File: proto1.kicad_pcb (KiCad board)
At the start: 2 copper layers, 75 x 51 mm, 67 parts, among them J1 12402012E212A, J11 TC2030, J12 PA_L, J13 Conn_01x02, J14 PA_L, J15 PA_L, J16 PA_L, J17 PA_L, J18 PA_L, J3 LCD, SW1 RESET, SW2 SW_SPDT, SW3 BOOT, SW4 USR1, SW5 USR2, U1 STM32G0B1CBTx, U3 AP2112K-3.3, U4 MCP6002-xMS, Y2 Crystal

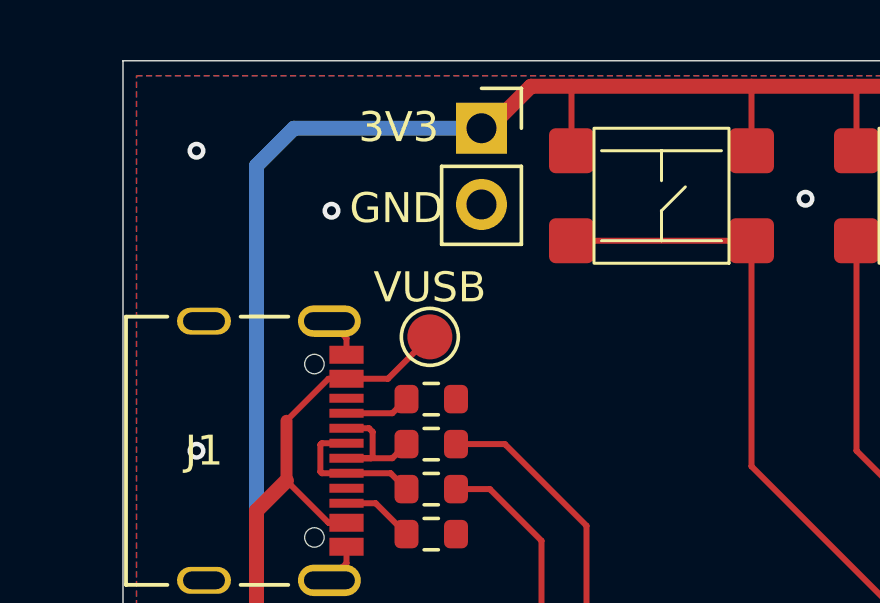
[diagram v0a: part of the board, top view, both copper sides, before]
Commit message: refactor hierarchical sheets to use sheet pins
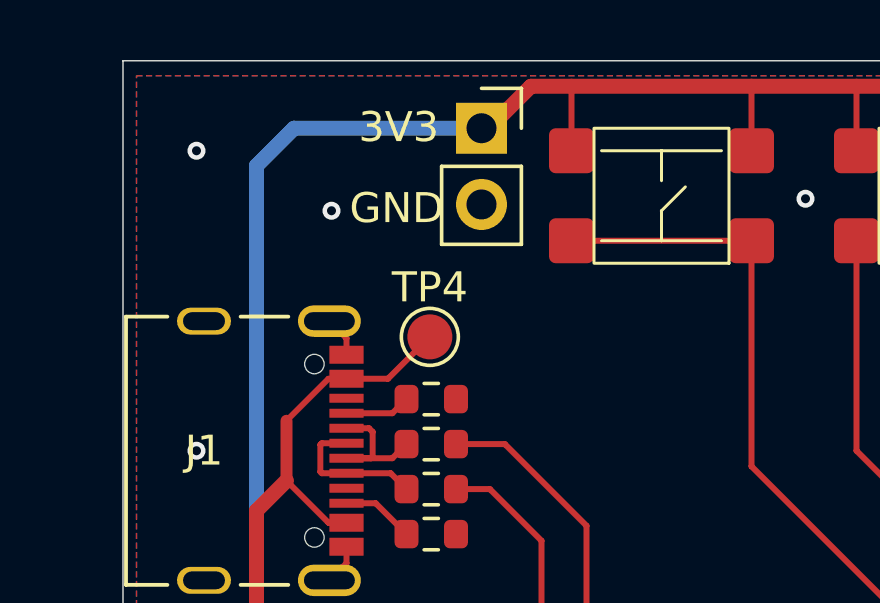
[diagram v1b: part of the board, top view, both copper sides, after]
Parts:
- renumbered VUSB to TP4

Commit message: WIP relayout of board
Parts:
- added AE1: ~, antenna:capacitive_coupled_50mmx8mm, F.Cu at (115.5, 75.5)
- added C17: ~, humidity_sensors:single_layer_comb_34T, B.Cu at (96.5, 57.4)
- C1, C10, C11, C12, C2, C4, C5, C6, C7, C8, C9: footprint Capacitor_SMD:C_0603_1608Metric -> Capacitor_SMD:C_0402_1005Metric
- C3: footprint Capacitor_SMD:C_0402_1005Metric_Pad0.74x0.62mm_HandSolder -> Capacitor_SMD:C_0402_1005Metric
- R1, R10, R11, R12, R13, R14, R15, R16, R18, R19, R2, R20, R21, R22, R23, R24, R3, R4, R5, R6, R8, R9: footprint Resistor_SMD:R_0603_1608Metric -> Resistor_SMD:R_0402_1005Metric
- moved J18 12.4 mm to (72.4, 96.6), turned to 90 degrees
- moved R16 10.0 mm to (93.3, 99.0), turned to 0 degrees
- moved C12 10.0 mm to (93.3, 90.0), turned to 0 degrees
- moved C11 8.05 mm to (98.4, 79.8), turned to 0 degrees
- moved C13 7.68 mm to (88.6, 92.4), turned to 180 degrees
- moved J17 7.65 mm to (69.4, 81.1)
- moved XTAL1 7.44 mm to (87.8, 90.3), turned to 0 degrees
- moved C16 7.23 mm to (83.8, 91.1), turned to 90 degrees
- moved C14 7.17 mm to (87.1, 88.2), turned to 0 degrees
- moved J12 6.99 mm to (84.0, 96.6)
- moved R12 6.90 mm to (102.5, 66.0), turned to 180 degrees
- moved C4 6.66 mm to (87.5, 65.8), turned to -90 degrees
- moved MK1 6.53 mm to (91.1, 65.8), turned to 180 degrees
- moved SW2 6.40 mm to (47.8, 85.6)
- moved J16 6.01 mm to (72.3, 72.5)
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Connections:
- net HUMIDITY_SENSE_COMB renamed /PA1
- net H_COMB_DRIVE renamed Net-(C17-in)
- net MIC_OUT_PDM renamed /PA6
- net NTC_VDIV renamed /PA2
- net SPI1_CLK renamed /PA5
- net cc_antenna_out renamed /PA0
- C7 pad 1: H_COMB_SENSE -> Net-(C17-out)
- J16 pad 6: HUMIDITY_DRIVE_COMB -> /PC6
- R14 pad 2: HUMIDITY_DRIVE_COMB -> /PB15
- U1 pad 30: HUMIDITY_DRIVE_COMB -> /PC6
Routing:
- net H_COMB_SENSE: track 441.7 -> 0.00 mm, vias 1 -> 0
- net Net-(C17-in): track 448.4 -> 24.1 mm
- net +3V3: track 313.7 -> 338.7 mm, vias 5 -> 13
- net Net-(C17-out): track 0.00 -> 12.5 mm, vias 0 -> 1
- net /NRST: track 54.3 -> 41.8 mm, vias 2 -> 0
- net /PA0: track 32.1 -> 20.4 mm
- net /PA2: track 51.0 -> 40.1 mm, vias 2 -> 0
- net HUMIDITY_DRIVE_COMB: track 10.4 -> 0.00 mm
- net /PA1: track 40.2 -> 31.7 mm, vias 2 -> 0
- net /PA13: track 17.0 -> 8.93 mm
- net /PD3: track 8.20 -> 16.2 mm
- net /BOOT0: track 53.5 -> 45.7 mm
- net /PC6: track 0.00 -> 7.48 mm
- net /PB15: track 7.45 -> 14.4 mm
- net /PC7: track 27.8 -> 34.2 mm
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- removed copper zone on F.Cu, net Net-(AE1-Signal)
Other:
- outline, holes or cut-outs redrawn
- board text added: "PA6"
- board text added: "PA7"
- board text added: "PB0"
- board text added: "PB1"
- board text added: "PB10"
- board text added: "PB11"
- board text added: "PB12"
- board text added: "PB2"
- board text removed: "Boot/SWCLK"
- board text removed: "NRST"
- board text removed: "SWDIO"

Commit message: Board V3
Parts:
- removed C5, C8: 0.1uF, Capacitor_SMD:C_0402_1005Metric
- added C18: 0.1uF, Capacitor_SMD:C_0402_1005Metric, F.Cu at (66.9, 56.8)
- added C19: 0.1uF, Capacitor_SMD:C_0402_1005Metric, F.Cu at (70.0, 56.8)
- added C20: 1uF, Capacitor_SMD:C_0402_1005Metric, F.Cu at (114.1, 64.2)
- added D4: D_TVS, KUU:SOD-882, F.Cu at (55.2, 60.5)
- added D5: LED, LED_SMD:LED_0603_1608Metric, F.Cu at (76.2, 63.2)
- added G***: LOGO, Graphics:crikeycon11_dice, F.Cu at (124.8, 57.8)
- added G***: LOGO, Graphics:gh_logo_cat, B.Cu at (126.2, 53.5)
- added J2: Conn_01x03, Connector_PinHeader_2.54mm:PinHeader_1x03_P2.54mm_Vertical, F.Cu at (59.1, 68.4)
- added Q1: DO2301E-Q, Package_TO_SOT_SMD:SOT-23, F.Cu at (57.1, 90.7)
- added Q2: DMMT5401, Package_TO_SOT_SMD:SOT-23-6, F.Cu at (57.1, 86.5)
- added R17: 100k, Resistor_SMD:R_0402_1005Metric, F.Cu at (114.1, 59.4)
- added R25: 10k, Resistor_SMD:R_0402_1005Metric, F.Cu at (93.6, 64.2)
- added R26: R_Photo, JCHL:SMD_3.6x2.4mm, F.Cu at (89.5, 64.2)
- added R7: 100k, Resistor_SMD:R_0402_1005Metric, F.Cu at (116.2, 59.4)
- added TP1: GND, TestPoint:TestPoint_Pad_1.0x1.0mm, F.Cu at (113.9, 96.0)
- added TP2: 1V6, TestPoint:TestPoint_Pad_1.0x1.0mm, F.Cu at (116.2, 64.5)
- added TP3: 3V3, TestPoint:TestPoint_Pad_1.0x1.0mm, F.Cu at (113.9, 98.0)
- added U5: USBLC6-2P6, Package_TO_SOT_SMD:SOT-666, F.Cu at (55.3, 63.5)
- added U6: LM321, Package_TO_SOT_SMD:SOT-23-5, F.Cu at (115.2, 61.8)
- BT1: footprint Battery:BatteryHolder_Keystone_2468_2xAAA -> battery:BatteryHolder_Keystone_2468_2xAAA
- C15, C16: value 18pF -> 15pF; footprint Capacitor_SMD:C_0402_1005Metric_Pad0.74x0.62mm_HandSolder -> Capacitor_SMD:C_0402_1005Metric
- D1: value D_Schottky -> D; footprint Diode_SMD:D_SOD-123 -> Diode_SMD:D_0402_1005Metric
- R12: value 100k -> 10k
- R18: value 100k -> 68k
- R19: value 100k -> 100Ω
- R4, R5: value 22R -> 10k
- TP4: value VBUS -> VBatt; footprint TestPoint:TestPoint_Pad_D1.5mm -> TestPoint:TestPoint_Pad_1.0x1.0mm
- U4: footprint Package_TO_SOT_SMD:SuperSOT-8 -> Package_SO:SOP-8_3.76x4.96mm_P1.27mm
- XTAL1: value ~ -> 8Mz CL=20pF
- Y2: value Crystal -> 32.768KHz 12.5pF 70kΩ; footprint Crystal:Crystal_SMD_0603-2Pin_6.0x3.5mm -> Crystal:Crystal_SMD_EuroQuartz_EQ161-2Pin_3.2x1.5mm
- moved R18 53.2 mm to (56.5, 82.7), turned to 0 degrees
- moved R13 50.3 mm to (54.7, 86.5), turned to -90 degrees
- moved R12 49.3 mm to (56.5, 83.8)
- moved TP4 36.0 mm to (53.5, 95.7)
- moved R19 30.4 mm to (76.2, 64.7), turned to 0 degrees
- moved R5 16.4 mm to (70.0, 57.9), turned to 180 degrees
- moved TP15 14.4 mm to (85.0, 52.5)
- moved C4 14.1 mm to (101.5, 65.4)
- moved C6 14.1 mm to (102.5, 65.4)
- moved R4 13.9 mm to (66.9, 57.9), turned to 0 degrees
- moved R14 13.6 mm to (85.1, 55.0)
- moved J11 13.4 mm to (55.3, 70.8)
- moved D2 11.1 mm to (52.4, 84.4), turned to -90 degrees
- moved TP14 10.8 mm to (110.2, 66.1)
- moved C17 10.8 mm to (107.3, 57.2)
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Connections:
- net /PC14 renamed /LSE_P
- net /PC15 renamed /LSE_N
- C1 pad 1: Net-(J1-VBUS) -> +5V
- C2 pad 1: Net-(D1-K) -> Net-(Q1-S)
- C7 pad 2: /PA1 -> /PA3
- D1 pad 1: Net-(D1-K) -> Net-(BT1-+)
- D1 pad 2: Net-(BT1-+) -> Net-(D1-A)
- J1 pad A4_B9: Net-(J1-VBUS) -> +5V
- J1 pad A6: Net-(J1-D+_A) -> D+
- J1 pad A7: Net-(J1-D-_A) -> D-
- J1 pad B4_A9: Net-(J1-VBUS) -> +5V
- J1 pad B6: Net-(J1-D+_A) -> D+
- J1 pad B7: Net-(J1-D-_A) -> D-
- R1 pad 1: Net-(J1-VBUS) -> +5V
- R10 pad 2: /PA2 -> /PA4
- R11 pad 1: /PA1 -> /PA3
- R11 pad 2: Net-(C5-Pad1) -> 1V6
- R12 pad 1: +3V3 -> Net-(D1-A)
- R12 pad 2: Net-(C5-Pad1) -> Net-(Q2B-B2)
- R13 pad 1: Net-(C5-Pad1) -> GND
- R13 pad 2: GND -> Net-(Q1-G)
- R18 pad 1: +3V3 -> GND
- R18 pad 2: Net-(C8-Pad1) -> Net-(D1-A)
- R19 pad 1: Net-(C8-Pad1) -> /PC6
- R19 pad 2: GND -> Net-(D5-A)
- R20 pad 1: Net-(C8-Pad1) -> 1V6
- R4 pad 1: D+ -> GND
- R4 pad 2: Net-(J1-D+_A) -> /PA10
- R5 pad 1: Net-(J1-D-_A) -> GND
- R5 pad 2: D- -> /PC7
- SW2 pad 2: Net-(D1-K) -> Net-(Q1-S)
- TH1 pad 1: /PA2 -> /PA4
- TP14 pad 1: /PA1 -> /PA3
- TP4 pad 1: Net-(J1-VBUS) -> Net-(BT1-+)
- U3 pad 1: Net-(J1-VBUS) -> +5V
- U3 pad 3: Net-(J1-VBUS) -> +5V
- U3 pad 5: Net-(D1-K) -> Net-(Q1-S)
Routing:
- net Net-(J1-VBUS): track 38.7 -> 0.00 mm
- net /PA4: track 6.88 -> 43.2 mm
- net /PA3: track 3.45 -> 35.6 mm
- net +5V: track 0.00 -> 30.0 mm
- net /PA2: track 40.1 -> 11.0 mm
- net Net-(Q1-S): track 0.00 -> 28.1 mm
- net /PA1: track 31.7 -> 7.98 mm
- net /NRST: track 41.8 -> 64.4 mm
- net /BOOT0: track 45.7 -> 66.4 mm
- net /PA13: track 8.93 -> 28.1 mm
- net 1V6: track 0.00 -> 14.7 mm
- net Net-(BT1-+): track 2.07 -> 14.2 mm
- net /PB15: track 14.4 -> 24.7 mm
- net Net-(C17-in): track 24.1 -> 14.3 mm
- net D+: track 28.0 -> 37.1 mm
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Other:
- board size 75 x 51 mm -> 85 x 51 mm
- board text added: "1V6"
- board text added: "BOOT SEL"
- board text added: "BTN1"
- board text added: "Botagar"
- board text added: "CRIKEYCON 11"
- board text added: "Cut Along Line To Isolate VREF"
- board text added: "HUMIDITY"
- board text added: "LIGHT"
- board text added: "MIC"
- board text added: "MODE"
- board text added: "NRST"
- board text added: "PA0"
- board text added: "PA1"
- board text added: "PA11/D-"
- board text added: "PA12/D+"
- board text added: "PA13/SWDIO"
- board text added: "PA14/SWCLK"
- board text added: "PA15"
- board text added: "PA2"
- board text added: "PA3"
- board text added: "PA4"
- board text added: "PA5"
- board text added: "PA8"
- board text added: "PA9"
- board text added: "PB13"
- board text added: "PB14"
- board text added: "PB15"
- board text added: "PB3"
- board text added: "PB4"
- board text added: "PB5"
- board text added: "PB6"
- board text added: "PB7"
- board text added: "PB8"
- board text added: "PB9"
- board text added: "PC13"
- board text added: "PC14"
- board text added: "PC15"
- board text added: "PC6"
- board text added: "PC7"
- board text added: "PCB By"
- board text added: "PD0"
- board text added: "PD1"
- board text added: "PD2"
- board text added: "PD3"
- board text added: "PF0"
- board text added: "PF1"
- board text added: "PF2/NRST"
- board text added: "RESET"
- board text added: "STM32G0B1"
- board text added: "SWCLK"
- board text added: "SWDIO"
- board text added: "TEMPS"
- board text added: "VREF"
- board text added: "WIRE"
